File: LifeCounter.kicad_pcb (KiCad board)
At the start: 2 copper layers, 200 parts, among them J201 USBC, J301 Debug, Q201 DO2308S, Q202 DO2309A, Q203 DO2309A, Q601 DO2309A, Q602 DO2309A, Q603 DO2309A, Q604 DO2309A, Q605 DO2309A, Q606 DO2309A, Q607 DO2309A, Q608 DO2309A, Q609 DO2308S, Q610 DO2308S, Q611 DO2308S, Q612 DO2308S, Q701 DO2309A, Q702 DO2309A, Q703 DO2309A, Q704 DO2309A, Q705 DO2309A, Q706 DO2309A, Q707 DO2309A, Q708 DO2309A, Q709 DO2308S, Q710 DO2308S, Q711 DO2308S, Q712 DO2308S, Q801 DO2308S, SW201 PWR_ON, SW301 RST, SW401 RotaryEncoder_Switch_MP, SW501 RotaryEncoder_Switch_MP, U201 TPS630701RNMR, U202 BQ24090DGQ, U203 BQ27441-G1, U301 STM32C031K6Tx, U401 74LVC3G14, U501 74LVC3G14, U601 74HC595, U603 CC56-12GWA, U604 74HC595, U701 74HC595, U703 CC56-12GWA, U704 74HC595

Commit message: Subcircuits routed
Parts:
- added TP601: DAT, TestPoint:TestPoint_Pad_D1.0mm, B.Cu at (159.3, 104.8)
- added TP602: CLK, TestPoint:TestPoint_Pad_D1.0mm, B.Cu at (156.8, 104.8)
- added TP603: ~CLR, TestPoint:TestPoint_Pad_D1.0mm, B.Cu at (149.1, 104.8)
- added TP604: LAT, TestPoint:TestPoint_Pad_D1.0mm, B.Cu at (154.2, 104.8)
- added TP605: ~OE, TestPoint:TestPoint_Pad_D1.0mm, B.Cu at (151.7, 104.8)
- added TP701: DAT, TestPoint:TestPoint_Pad_D1.0mm, B.Cu at (148.2, 74.8)
- added TP702: CLK, TestPoint:TestPoint_Pad_D1.0mm, B.Cu at (150.7, 74.8)
- added TP703: ~CLR, TestPoint:TestPoint_Pad_D1.0mm, B.Cu at (158.4, 74.8)
- added TP704: LAT, TestPoint:TestPoint_Pad_D1.0mm, B.Cu at (153.3, 74.8)
- added TP705: ~OE, TestPoint:TestPoint_Pad_D1.0mm, B.Cu at (155.8, 74.8)
- C301, C302, C303, C304, C401, C402, C403, C404, C501, C502, C503, C504, C701, C702, D301, J301, Q701, Q702, Q703, Q704, Q705, Q706, Q707, Q708, Q709, Q710, Q711, Q712, R301, R302, R303, R304, R305, R306, R401, R402, R403, R404, R405, R406, R501, R502, R503, R504, R505, R506, R701, R702, R703, R704, R705, R706, R707, R708, R709, R710, R711, R712, R713, R714, R715, R716, R717, R718, R719, R720, R721, R722, R723, R724, TP301, TP302, TP303, TP304, TP401, TP402, TP403, TP501, TP502, TP503, U401, U501, U701, U704: moved to B.Cu
- moved R402 237.6 mm to (197.5, 122.7), turned to 180 degrees
- moved SW401 234.1 mm to (201.0, 118.8), turned to 180 degrees
- moved R405 231.5 mm to (198.7, 118.7), turned to -90 degrees
- moved R403 229.3 mm to (197.5, 109.8), turned to 180 degrees
- moved R406 227.5 mm to (198.7, 113.6), turned to 90 degrees
- moved R404 226.5 mm to (189.2, 121.5), turned to 180 degrees
- moved R401 226.2 mm to (189.2, 111.0)
- moved C503 224.6 mm to (111.3, 60.8), turned to 90 degrees
- moved C504 223.6 mm to (111.3, 65.9), turned to -90 degrees
- moved U501 223.0 mm to (116.3, 63.3)
- moved C403 219.6 mm to (196.2, 118.7), turned to -90 degrees
- moved C601 219.3 mm to (178.5, 118.8)
- moved C602 219.3 mm to (130.0, 114.0)
- moved D601 219.3 mm to (122.7, 108.7)
- moved D602 219.3 mm to (122.7, 113.7)
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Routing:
- net Net-(Q712-G): track 0.00 -> 67.9 mm, vias 0 -> 2
- net /Display2/~{CLR}: track 0.00 -> 67.2 mm, vias 0 -> 3
- net /Display2/LAT: track 0.00 -> 65.8 mm, vias 0 -> 3
- net /Display1/~{OE}: track 70.5 -> 133.5 mm, vias 4 -> 8
- net /Display1/CLK: track 72.5 -> 131.2 mm, vias 2 -> 4
- net VCC: track 65.9 -> 121.9 mm, vias 26 -> 42
- net Net-(U701-QH'): track 0.00 -> 55.8 mm, vias 0 -> 2
- net Net-(Q711-G): track 0.00 -> 47.0 mm, vias 0 -> 2
- net Net-(Q701-G): track 0.00 -> 44.2 mm, vias 0 -> 2
- net Net-(Q705-G): track 0.00 -> 41.5 mm, vias 0 -> 2
- net Net-(Q704-G): track 0.00 -> 34.7 mm, vias 0 -> 2
- net /Display1/DAT: track 33.9 -> 68.5 mm, vias 1 -> 4
- net Net-(Q706-G): track 0.00 -> 34.0 mm, vias 0 -> 2
- net Net-(D701-A): track 0.00 -> 24.0 mm, vias 0 -> 1
- net /Display2/Digit1: track 0.00 -> 22.9 mm, vias 0 -> 1
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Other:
- board outline added: 100.2 x 74.8 mm

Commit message: Everything routed :)
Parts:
- D301: moved to F.Cu
- moved C301 104.1 mm to (110.1, 121.2), turned to 90 degrees
- moved D301 93.3 mm to (108.1, 79.2), turned to 0 degrees
- moved H901 86.0 mm to (118.7, 72.8)
- moved H904 79.9 mm to (189.3, 72.8)
- moved R302 79.1 mm to (108.1, 79.2), turned to 180 degrees
- moved R301 70.8 mm to (115.1, 121.1)
- moved C302 45.8 mm to (157.4, 87.4), turned to 90 degrees
- moved C303 42.7 mm to (159.7, 87.8), turned to 90 degrees
- moved C304 40.5 mm to (162.0, 87.4), turned to 90 degrees
- moved R304 32.5 mm to (159.2, 96.2), turned to 180 degrees
- moved TP304 32.1 mm to (168.8, 96.0)
- moved TP302 32.1 mm to (162.7, 96.1)
- moved TP303 31.4 mm to (166.6, 96.0)
- moved TP301 29.9 mm to (162.7, 93.1)
- moved R303 29.4 mm to (159.2, 93.7), turned to 180 degrees
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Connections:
- U301 pad 10: /Display1/LAT -> /Display2/LAT
- U301 pad 11: /Display1/~{CLR} -> /Display2/~{CLR}
- U301 pad 15: /Controller/Encoder2.CLK -> /Controller/Encoder1.CLK
- U301 pad 16: /Controller/Encoder2.DAT -> /Controller/Encoder1.DAT
- U301 pad 17: /Controller/Encoder2.BTN -> /Controller/Encoder1.BTN
- U301 pad 27: /Display2/LAT -> /Display1/LAT
- U301 pad 28: /Display2/~{CLR} -> /Display1/~{CLR}
- U301 pad 7: /Controller/Encoder1.CLK -> /Controller/Encoder2.CLK
- U301 pad 8: /Controller/Encoder1.DAT -> /Controller/Encoder2.DAT
- U301 pad 9: /Controller/Encoder1.BTN -> /Controller/Encoder2.BTN
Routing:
- net /Controller/~{RST}: track 0.00 -> 124.7 mm, vias 0 -> 5
- net /Controller/I2C1.SDA: track 0.00 -> 78.3 mm, vias 0 -> 2
- net /Controller/I2C1.SCL: track 0.00 -> 76.0 mm, vias 0 -> 2
- net /Controller/Heartbeat: track 0.00 -> 70.1 mm, vias 0 -> 1
- net /Controller/PWR_OK: track 2.46 -> 69.5 mm, vias 0 -> 2
- net /Controller/Encoder2.CLK: track 6.67 -> 66.3 mm, vias 2 -> 5
- net /Power/EN: track 7.55 -> 66.3 mm, vias 1 -> 2
- net /Controller/Encoder2.BTN: track 8.93 -> 64.7 mm, vias 2 -> 5
- net /Controller/Encoder2.DAT: track 6.86 -> 60.9 mm, vias 2 -> 5
- net /Display1/~{OE}: track 133.5 -> 185.9 mm, vias 8 -> 14
- net /Display1/CLK: track 131.2 -> 180.6 mm, vias 4 -> 10
- net /Display1/DAT: track 68.5 -> 117.9 mm, vias 4 -> 10
- net /Power/VIN: track 15.6 -> 59.6 mm, vias 30 -> 32
- net /Controller/Encoder1.CLK: track 6.67 -> 46.4 mm, vias 2 -> 4
- net /Buzzer/Buzz: track 2.87 -> 41.9 mm, vias 0 -> 2
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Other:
- board size 100.2 x 74.8 mm -> 100 x 74.8 mm

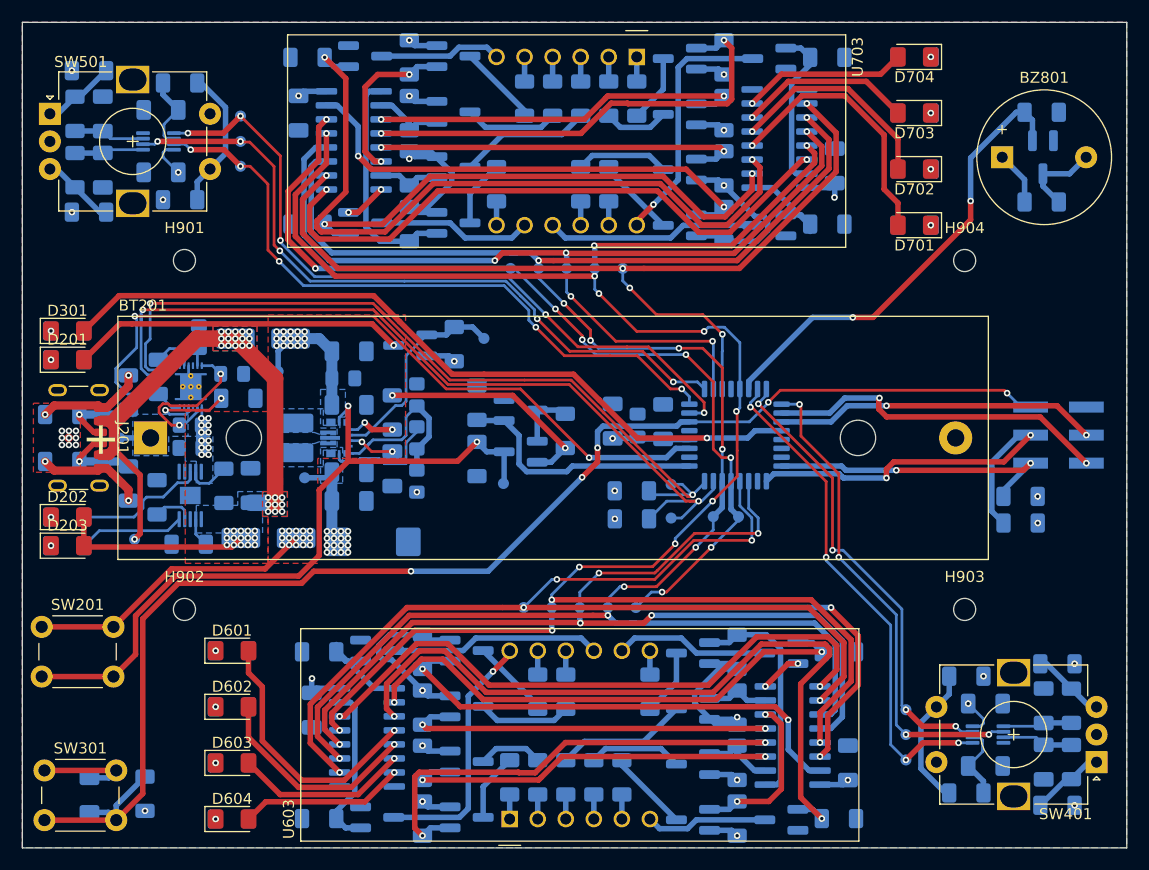
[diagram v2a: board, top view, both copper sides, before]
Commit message: Move silkscreen text to comments layer
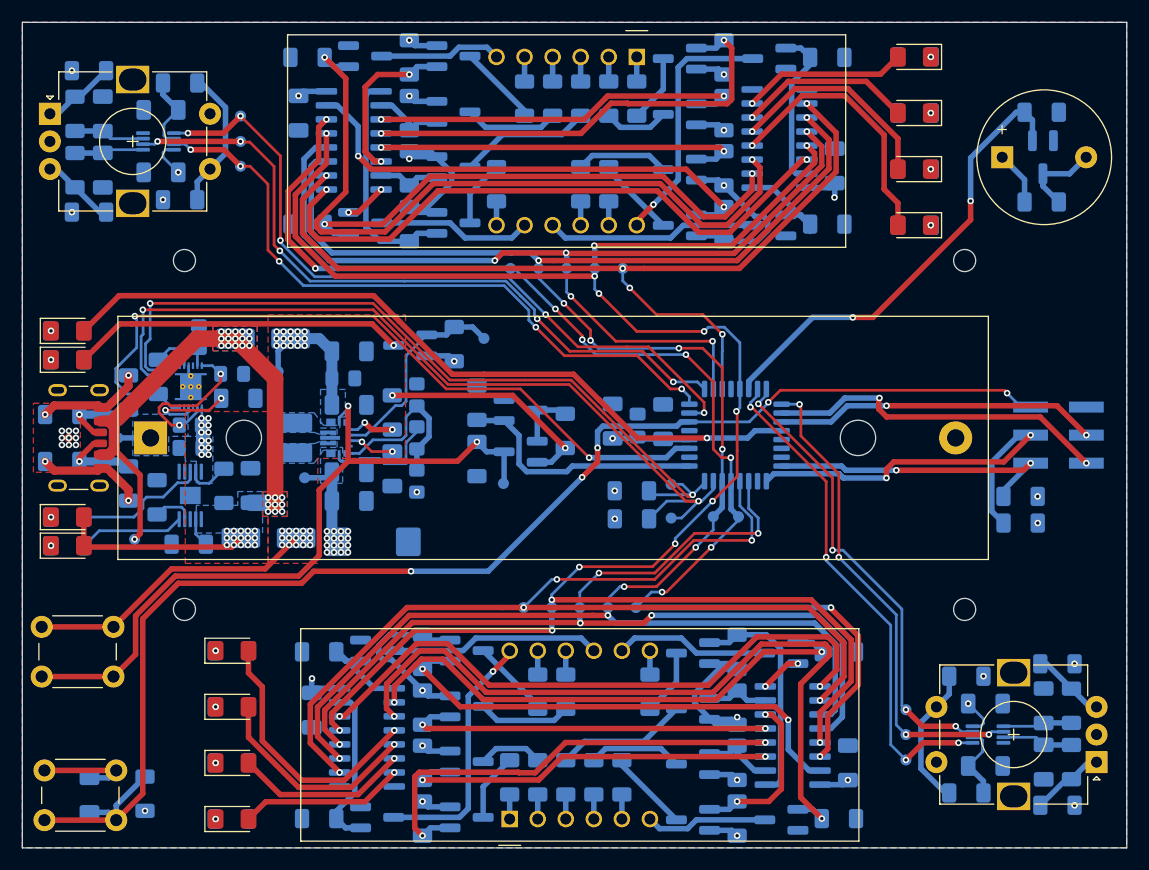
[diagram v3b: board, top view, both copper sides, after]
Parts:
- moved TP205 0.16 mm to (112.7, 88.9)
- moved L201 0.10 mm to (128.4, 88.9)
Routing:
- net /Controller/I2C1.SCL: track 76.0 -> 75.0 mm
- net /Display1/CLK: track 180.6 -> 179.8 mm
